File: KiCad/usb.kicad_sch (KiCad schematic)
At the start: 4 parts, among them J16 RJE361882415, J19 USB3_A_Stacked, J20 USB3_IDC, J21 Conn_02x05_Odd_Even

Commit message: Re-annotate components
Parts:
- renumbered J16 to J19, J19 to J22, J20 to J23, J21 to J24
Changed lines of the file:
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@@
 		(dnp no)
 		(fields_autoplaced yes)
-		(property "Reference" "#PWR0219"
+		(property "Reference" "#PWR0273"
 			(at 80.01 59.69 0)
 			(effects
@@
 			(project ""
 				(path "/49abeb3a-c598-45a3-ba6b-595eb04f17a8/aeaf6077-b212-49fa-a33e-8ac7d8738247"
-					(reference "#PWR0219")
+					(reference "#PWR0273")
 					(unit 1)
 				)
@@
 		(on_board yes)
 		(dnp no)
-		(property "Reference" "#PWR0232"
+		(property "Reference" "#PWR0284"
 			(at 248.92 87.63 0)
 			(effects
@@
 			(project "LattePandaMuCluster"
 				(path "/49abeb3a-c598-45a3-ba6b-595eb04f17a8/aeaf6077-b212-49fa-a33e-8ac7d8738247"
-					(reference "#PWR0232")
+					(reference "#PWR0284")
 					(unit 1)
 				)
@@
 		(on_board yes)
 		(dnp no)
-		(property "Reference" "#PWR0228"
+		(property "Reference" "#PWR0276"
 			(at 162.56 78.74 0)
 			(effects
@@
 			(project "LattePandaMuCluster"
 				(path "/49abeb3a-c598-45a3-ba6b-595eb04f17a8/aeaf6077-b212-49fa-a33e-8ac7d8738247"
-					(reference "#PWR0228")
+					(reference "#PWR0276")
 					(unit 1)
 				)
@@
 		(on_board yes)
 		(dnp no)
-		(property "Reference" "#PWR0231"
+		(property "Reference" "#PWR0282"
 			(at 220.98 87.63 0)
 			(effects
@@
 			(project "LattePandaMuCluster"
 				(path "/49abeb3a-c598-45a3-ba6b-595eb04f17a8/aeaf6077-b212-49fa-a33e-8ac7d8738247"
-					(reference "#PWR0231")
+					(reference "#PWR0282")
 					(unit 1)
 				)
@@
 		(dnp no)
 		(fields_autoplaced yes)
-		(property "Reference" "#PWR0221"
+		(property "Reference" "#PWR0275"
 			(at 83.82 163.83 0)
 			(effects
@@
 			(project "LattePandaMuCluster"
 				(path "/49abeb3a-c598-45a3-ba6b-595eb04f17a8/aeaf6077-b212-49fa-a33e-8ac7d8738247"
-					(reference "#PWR0221")
+					(reference "#PWR0275")
 					(unit 1)
 				)
@@
 		(on_board yes)
 		(dnp no)
-		(property "Reference" "#PWR0229"
+		(property "Reference" "#PWR0272"
 			(at 69.85 129.54 0)
 			(effects
@@
 			(project "LattePandaMuCluster"
 				(path "/49abeb3a-c598-45a3-ba6b-595eb04f17a8/aeaf6077-b212-49fa-a33e-8ac7d8738247"
-					(reference "#PWR0229")
+					(reference "#PWR0272")
 					(unit 1)
 				)
@@
 		(dnp no)
 		(fields_autoplaced yes)
-		(property "Reference" "J16"
+		(property "Reference" "J19"
 			(at 189.23 32.3849 0)
 			(effects
@@
 			(project "LattePandaMuCluster"
 				(path "/49abeb3a-c598-45a3-ba6b-595eb04f17a8/aeaf6077-b212-49fa-a33e-8ac7d8738247"
-					(reference "J16")
+					(reference "J19")
 					(unit 3)
 				)
@@
 		(on_board yes)
 		(dnp no)
-		(property "Reference" "#PWR0226"
+		(property "Reference" "#PWR0277"
 			(at 163.83 25.4 0)
 			(effects
@@
 			(project "LattePandaMuCluster"
 				(path "/49abeb3a-c598-45a3-ba6b-595eb04f17a8/aeaf6077-b212-49fa-a33e-8ac7d8738247"
-					(reference "#PWR0226")
+					(reference "#PWR0277")
 					(unit 1)
 				)
@@
 		(on_board yes)
 		(dnp no)
-		(property "Reference" "J19"
+		(property "Reference" "J22"
 			(at 176.53 67.31 0)
 			(effects
@@
 			(project ""
 				(path "/49abeb3a-c598-45a3-ba6b-595eb04f17a8/aeaf6077-b212-49fa-a33e-8ac7d8738247"
-					(reference "J19")
+					(reference "J22")
 					(unit 2)
 				)
@@
 		(on_board yes)
 		(dnp no)
-		(property "Reference" "#PWR0227"
+		(property "Reference" "#PWR0271"
 			(at 69.85 76.2 0)
 			(effects
@@
 			(project "LattePandaMuCluster"
 				(path "/49abeb3a-c598-45a3-ba6b-595eb04f17a8/aeaf6077-b212-49fa-a33e-8ac7d8738247"
-					(reference "#PWR0227")
+					(reference "#PWR0271")
 					(unit 1)
 				)
@@
 		(dnp no)
 		(fields_autoplaced yes)
-		(property "Reference" "J16"
+		(property "Reference" "J19"
 			(at 91.44 32.3849 0)
 			(effects
@@
 			(project "LattePandaMuCluster"
 				(path "/49abeb3a-c598-45a3-ba6b-595eb04f17a8/aeaf6077-b212-49fa-a33e-8ac7d8738247"
-					(reference "J16")
+					(reference "J19")
 					(unit 2)
 				)
@@
 		(dnp no)
 		(fields_autoplaced yes)
-		(property "Reference" "#PWR0222"
+		(property "Reference" "#PWR0281"
 			(at 181.61 163.83 0)
 			(effects
@@
 			(project "LattePandaMuCluster"
 				(path "/49abeb3a-c598-45a3-ba6b-595eb04f17a8/aeaf6077-b212-49fa-a33e-8ac7d8738247"
-					(reference "#PWR0222")
+					(reference "#PWR0281")
 					(unit 1)
 				)
@@
 		(dnp no)
 		(fields_autoplaced yes)
-		(property "Reference" "#PWR0224"
+		(property "Reference" "#PWR0279"
 			(at 176.53 113.03 0)
 			(effects
@@
 			(project "LattePandaMuCluster"
 				(path "/49abeb3a-c598-45a3-ba6b-595eb04f17a8/aeaf6077-b212-49fa-a33e-8ac7d8738247"
-					(reference "#PWR0224")
+					(reference "#PWR0279")
 					(unit 1)
 				)
@@
 		(dnp no)
 		(fields_autoplaced yes)
-		(property "Reference" "#PWR0223"
+		(property "Reference" "#PWR0274"
 			(at 83.82 110.49 0)
 			(effects
@@
 			(project "LattePandaMuCluster"
 				(path "/49abeb3a-c598-45a3-ba6b-595eb04f17a8/aeaf6077-b212-49fa-a33e-8ac7d8738247"
-					(reference "#PWR0223")
+					(reference "#PWR0274")
 					(unit 1)
 				)
@@
 		(dnp no)
 		(fields_autoplaced yes)
-		(property "Reference" "J20"
+		(property "Reference" "J23"
 			(at 95.25 136.5249 0)
 			(effects
@@
 			(project ""
 				(path "/49abeb3a-c598-45a3-ba6b-595eb04f17a8/aeaf6077-b212-49fa-a33e-8ac7d8738247"
-					(reference "J20")
+					(reference "J23")
 					(unit 1)
 				)
@@
 		(dnp no)
 		(fields_autoplaced yes)
-		(property "Reference" "J21"
+		(property "Reference" "J24"
 			(at 234.95 78.74 0)
 			(effects
@@
 			(project ""
 				(path "/49abeb3a-c598-45a3-ba6b-595eb04f17a8/aeaf6077-b212-49fa-a33e-8ac7d8738247"
-					(reference "J21")
+					(reference "J24")
 					(unit 1)
 				)
@@
 		(dnp no)
 		(fields_autoplaced yes)
-		(property "Reference" "#PWR0220"
+		(property "Reference" "#PWR0280"
 			(at 177.8 59.69 0)
 			(effects
@@
 			(project "LattePandaMuCluster"
 				(path "/49abeb3a-c598-45a3-ba6b-595eb04f17a8/aeaf6077-b212-49fa-a33e-8ac7d8738247"
-					(reference "#PWR0220")
+					(reference "#PWR0280")
 					(unit 1)
 				)
@@
 		(dnp no)
 		(fields_autoplaced yes)
-		(property "Reference" "#PWR0233"
+		(property "Reference" "#PWR0283"
 			(at 234.95 106.68 0)
 			(effects
@@
 			(project ""
 				(path "/49abeb3a-c598-45a3-ba6b-595eb04f17a8/aeaf6077-b212-49fa-a33e-8ac7d8738247"
-					(reference "#PWR0233")
+					(reference "#PWR0283")
 					(unit 1)
 				)
@@
 		(dnp no)
 		(fields_autoplaced yes)
-		(property "Reference" "J20"
+		(property "Reference" "J23"
 			(at 193.04 136.5249 0)
 			(effects
@@
 			(project ""
 				(path "/49abeb3a-c598-45a3-ba6b-595eb04f17a8/aeaf6077-b212-49fa-a33e-8ac7d8738247"
-					(reference "J20")
+					(reference "J23")
 					(unit 2)
 				)
@@
 		(on_board yes)
 		(dnp no)
-		(property "Reference" "#PWR0230"
+		(property "Reference" "#PWR0278"
 			(at 167.64 129.54 0)
 			(effects
@@
 			(project "LattePandaMuCluster"
 				(path "/49abeb3a-c598-45a3-ba6b-595eb04f17a8/aeaf6077-b212-49fa-a33e-8ac7d8738247"
-					(reference "#PWR0230")
+					(reference "#PWR0278")
 					(unit 1)
 				)
@@
 		(on_board yes)
 		(dnp no)
-		(property "Reference" "J19"
+		(property "Reference" "J22"
 			(at 83.82 64.77 0)
 			(effects
@@
 			(project ""
 				(path "/49abeb3a-c598-45a3-ba6b-595eb04f17a8/aeaf6077-b212-49fa-a33e-8ac7d8738247"
-					(reference "J19")
+					(reference "J22")
 					(unit 1)
 				)
@@
 		(on_board yes)
 		(dnp no)
-		(property "Reference" "#PWR0225"
+		(property "Reference" "#PWR0270"
 			(at 66.04 25.4 0)
 			(effects
@@
 			(project ""
 				(path "/49abeb3a-c598-45a3-ba6b-595eb04f17a8/aeaf6077-b212-49fa-a33e-8ac7d8738247"
-					(reference "#PWR0225")
-					(unit 1)
-				)
+					(reference "#PWR0270")
+					(unit 1)
+				)

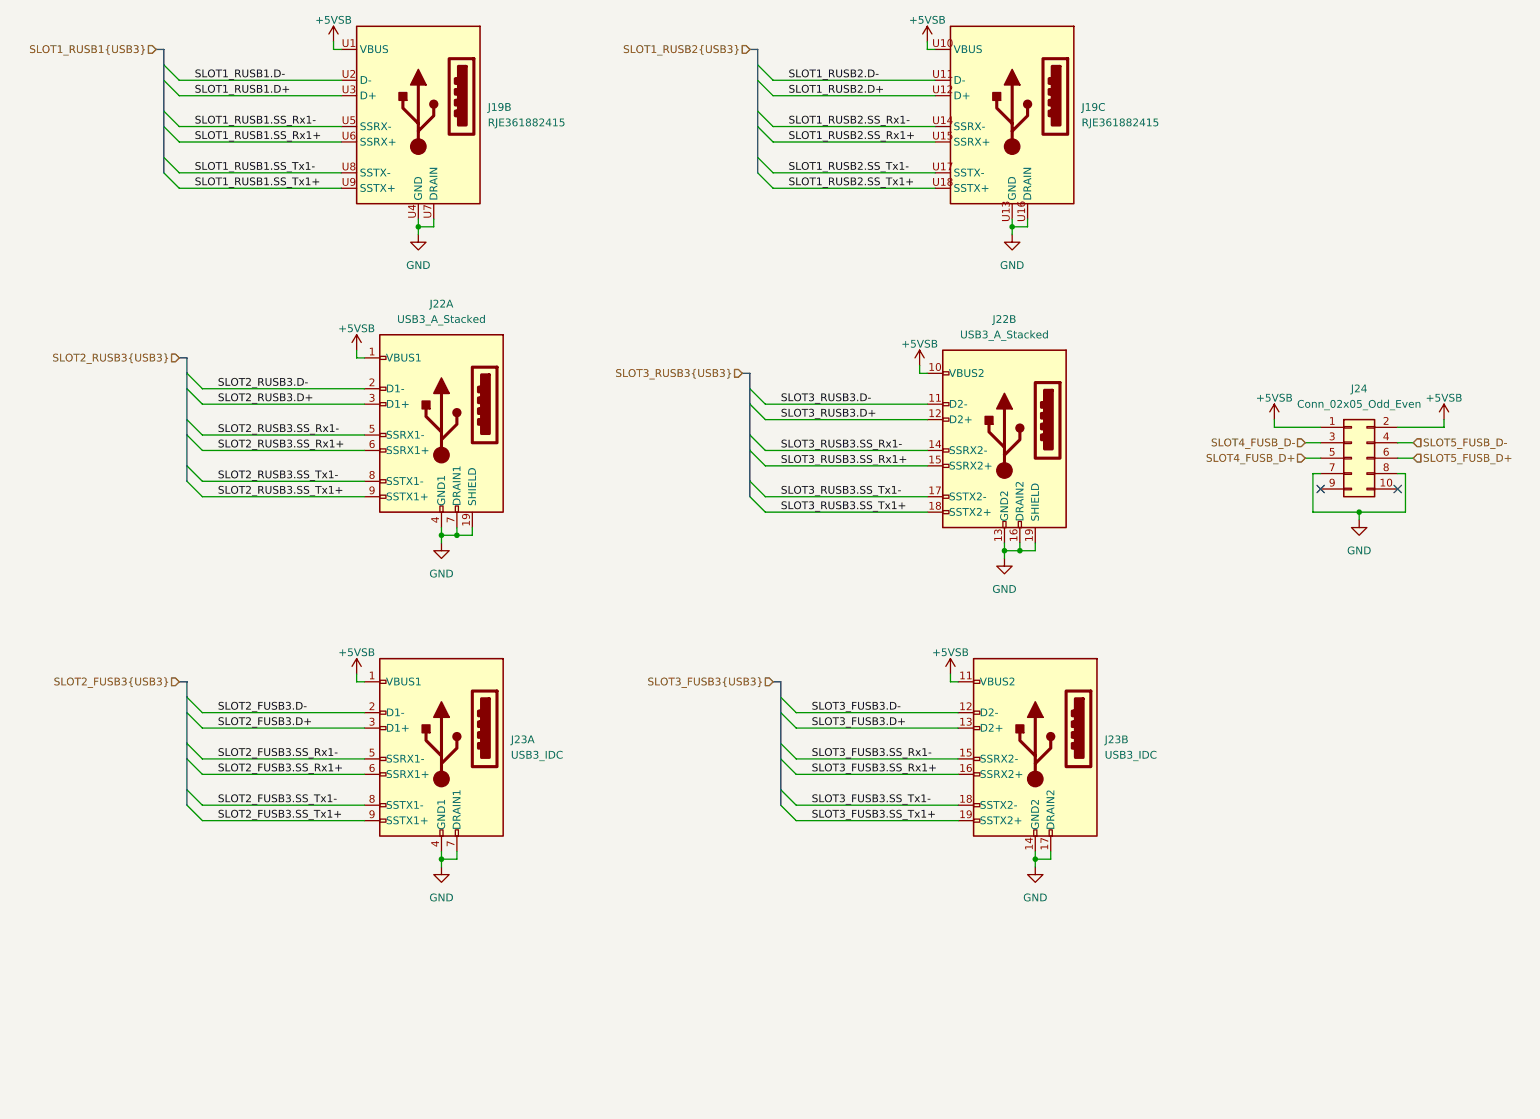
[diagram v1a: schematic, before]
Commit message: Add TVS diodes for ESD protection
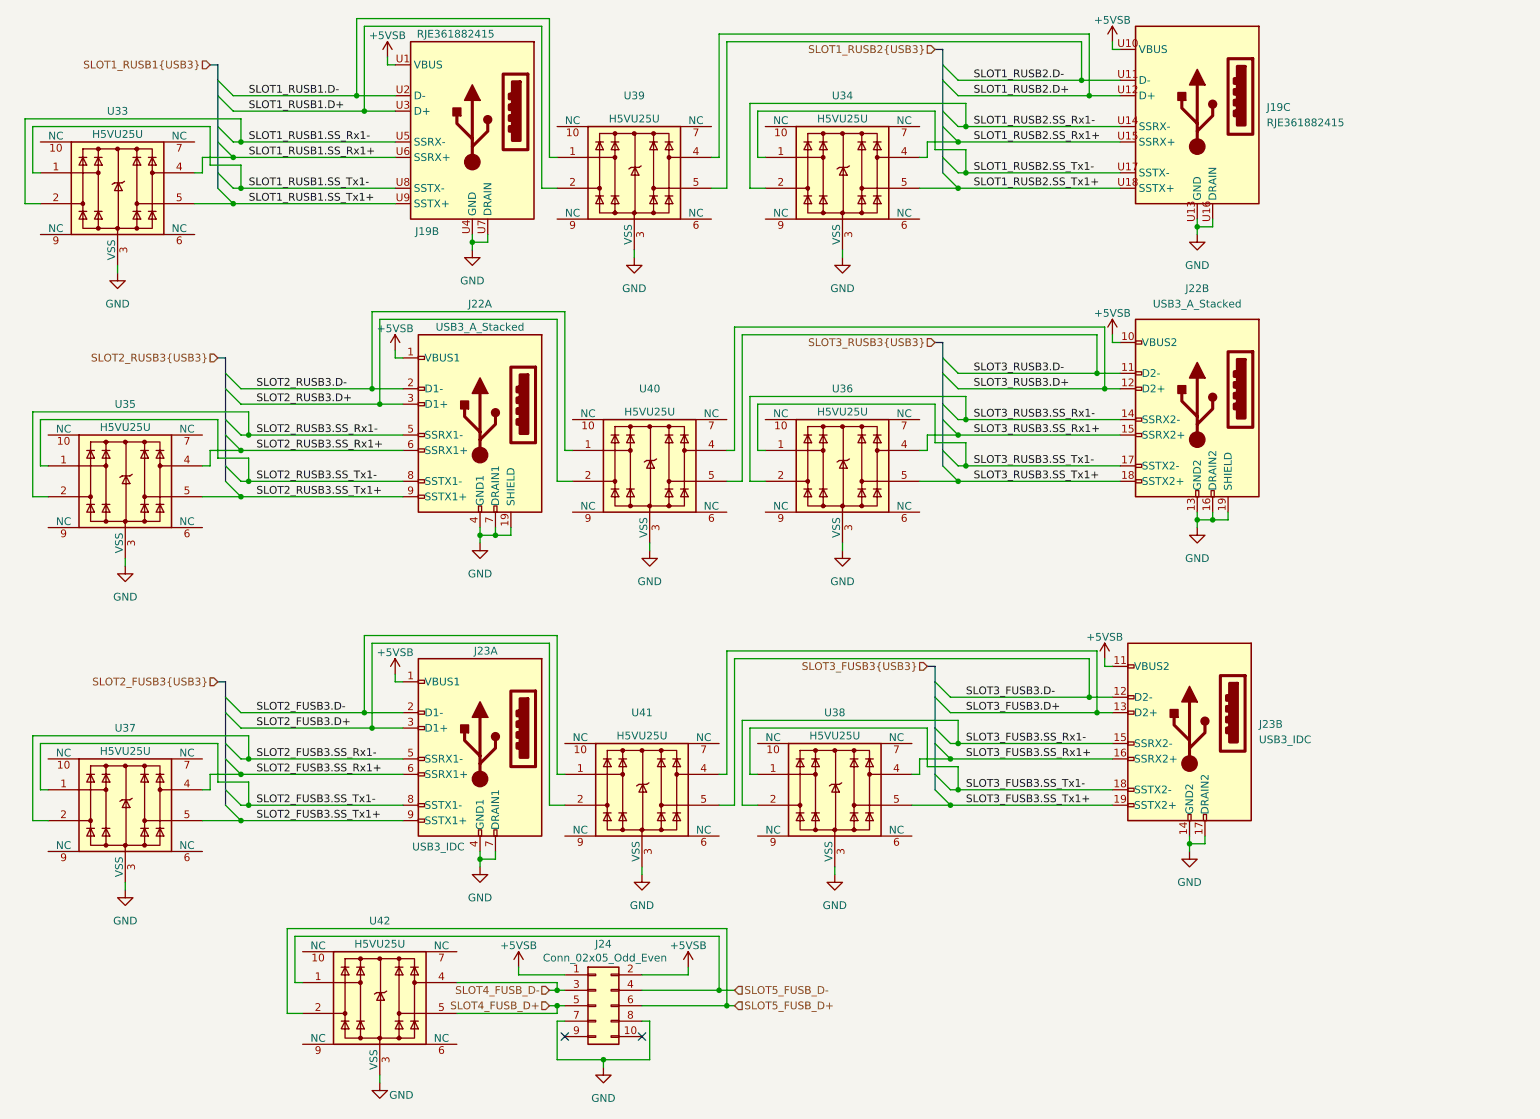
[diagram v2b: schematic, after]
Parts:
- added U33, U34, U35, U36, U37, U38, U39, U40, U41, U42: H5VU25U, Package_DFN_QFN:Diodes_UDFN-10_1.0x2.5mm_P0.5mm, symbol Power_Protection:D3V3XA4B10LP
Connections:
- net GND: now also U33.3 (VSS), U33.8 (VSS), U34.3 (VSS), U34.8 (VSS), U35.3 (VSS), U35.8 (VSS), U36.3 (VSS), U36.8 (VSS), U37.3 (VSS), U37.8 (VSS), U38.3 (VSS), U38.8 (VSS), U39.3 (VSS), U39.8 (VSS), U40.3 (VSS), U40.8 (VSS), U41.3 (VSS), U41.8 (VSS), U42.3 (VSS), U42.8 (VSS)
- net SLOT1_RUSB1.D+: now also U39.2
- net SLOT1_RUSB1.D-: now also U39.1
- net SLOT1_RUSB1.SS_Rx1+: now also U33.4
- net SLOT1_RUSB1.SS_Rx1-: now also U33.2
- net SLOT1_RUSB1.SS_Tx1+: now also U33.5
- net SLOT1_RUSB1.SS_Tx1-: now also U33.1
- net SLOT1_RUSB2.D+: now also U39.4
- net SLOT1_RUSB2.D-: now also U39.5
- net SLOT1_RUSB2.SS_Rx1+: now also U34.4
- net SLOT1_RUSB2.SS_Rx1-: now also U34.2
- net SLOT1_RUSB2.SS_Tx1+: now also U34.5
- net SLOT1_RUSB2.SS_Tx1-: now also U34.1
- net SLOT2_FUSB3.D+: now also U41.2
- net SLOT2_FUSB3.D-: now also U41.1
- net SLOT2_FUSB3.SS_Rx1+: now also U37.4
- net SLOT2_FUSB3.SS_Rx1-: now also U37.2
- net SLOT2_FUSB3.SS_Tx1+: now also U37.5
- net SLOT2_FUSB3.SS_Tx1-: now also U37.1
- net SLOT2_RUSB3.D+: now also U40.2
- net SLOT2_RUSB3.D-: now also U40.1
- net SLOT2_RUSB3.SS_Rx1+: now also U35.4
- net SLOT2_RUSB3.SS_Rx1-: now also U35.2
- net SLOT2_RUSB3.SS_Tx1+: now also U35.5
- net SLOT2_RUSB3.SS_Tx1-: now also U35.1
- net SLOT3_FUSB3.D+: now also U41.4
- net SLOT3_FUSB3.D-: now also U41.5
- net SLOT3_FUSB3.SS_Rx1+: now also U38.4
- net SLOT3_FUSB3.SS_Rx1-: now also U38.2
- net SLOT3_FUSB3.SS_Tx1+: now also U38.5
- net SLOT3_FUSB3.SS_Tx1-: now also U38.1
- net SLOT3_RUSB3.D+: now also U40.4
- net SLOT3_RUSB3.D-: now also U40.5
- net SLOT3_RUSB3.SS_Rx1+: now also U36.4
- net SLOT3_RUSB3.SS_Rx1-: now also U36.2
- net SLOT3_RUSB3.SS_Tx1+: now also U36.5
- net SLOT3_RUSB3.SS_Tx1-: now also U36.1
- net SLOT4_FUSB_D+: now also U42.5
- net SLOT4_FUSB_D-: now also U42.4
- net SLOT5_FUSB_D+: now also U42.2
- net SLOT5_FUSB_D-: now also U42.1
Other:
- moved on the sheet: J19B, J19C, J22A, J22B, J23A, J23B, J24

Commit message: Fix esd diodes, add some footprints.
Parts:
- J19: footprint (none) -> RJE361882145:AMPHENOL_RJE361882415
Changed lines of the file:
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@@
 			)
 		)
-		(property "Footprint" ""
+		(property "Footprint" "RJE361882145:AMPHENOL_RJE361882415"
 			(at 208.28 17.78 0)
 			(effects
@@
 			)
 		)
-		(property "Footprint" ""
+		(property "Footprint" "RJE361882145:AMPHENOL_RJE361882415"
 			(at 88.9 20.32 0)
 			(effects

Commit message: Add more footprints
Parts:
- removed J24: Conn_02x05_Odd_Even, symbol Connector_Generic:Conn_02x05_Odd_Even
- added J24: Conn_01x05, Connector_PinHeader_2.54mm:PinHeader_1x05_P2.54mm_Vertical, symbol Connector_Generic:Conn_01x05
- added J27: Conn_01x04, Connector_PinHeader_2.54mm:PinHeader_1x04_P2.54mm_Vertical, symbol Connector_Generic:Conn_01x04
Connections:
- net +5VSB: now also J24.1 (Pin_1), J27.1 (Pin_1)
- net GND: now also J24.4 (Pin_4), J27.4 (Pin_4)
- net SLOT4_FUSB_D+: now also J24.3 (Pin_3)
- net SLOT4_FUSB_D-: now also J24.2 (Pin_2)
- net SLOT5_FUSB_D+: now also J27.3 (Pin_3)
- net SLOT5_FUSB_D-: now also J27.2 (Pin_2)
- no-connect marks 2 -> 1
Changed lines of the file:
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@@
 	)
 	(no_connect
-		(at 116.84 185.42)
-	)
-	(no_connect
 		(at 104.14 185.42)
 	)
@@
 	)
 	(symbol
+		(lib_id "Connector_Generic:Conn_01x05")
+		(at 109.22 180.34 0)
+		(unit 1)
+		(exclude_from_sim no)
+		(in_bom yes)
+		(on_board yes)
+		(dnp no)
+		(property "Reference" "J24"
+			(at 110.49 185.928 0)
+			(effects
+				(font
+					(size 1.27 1.27)
+				)
+				(justify left)
+			)
+		)
+		(property "Value" "Conn_01x05"
+			(at 103.378 187.96 0)
+			(effects
+				(font
+					(size 1.27 1.27)
+				)
+				(justify left)
+			)
+		)
+		(property "Footprint" "Connector_PinHeader_2.54mm:PinHeader_1x05_P2.54mm_Vertical"
+			(at 109.22 180.34 0)
+			(effects
+				(font
+					(size 1.27 1.27)
+				)
+				(hide yes)
+			)
+		)
+		(property "Datasheet" "~"
+			(at 109.22 180.34 0)
+			(effects
+				(font
+					(size 1.27 1.27)
+				)
+				(hide yes)
+			)
+		)
+		(property "Description" "Generic connector, single row, 01x05, script generated (kicad-library-utils/schlib/autogen/connector/)"
+			(at 109.22 180.34 0)
+			(effects
+				(font
+					(size 1.27 1.27)
+				)
+				(hide yes)
+			)
+		)
+		(pin "3"
+		)
+		(pin "4"
+		)
+		(pin "2"
+		)
+		(pin "1"
+		)
+		(pin "5"
+		)
+		(instances
+			(project ""
+				(path "/49abeb3a-c598-45a3-ba6b-595eb04f17a8/aeaf6077-b212-49fa-a33e-8ac7d8738247"
+					(reference "J24")
+					(unit 1)
+				)
+			)
+		)
+	)
+	(symbol
 		(lib_id "power:+5V")
 		(at 124.46 173.99 0)
@@
 	)
 	(symbol
-		(lib_id "Connector_Generic:Conn_02x05_Odd_Even")
-		(at 109.22 180.34 0)
+		(lib_id "Connector_Generic:Conn_01x04")
+		(at 111.76 177.8 0)
+		(mirror y)
 		(unit 1)
 		(exclude_from_sim no)
@@
 		(on_board yes)
 		(dnp no)
-		(property "Reference" "J24"
-			(at 110.49 170.18 0)
+		(property "Reference" "J27"
+			(at 110.744 170.942 0)
 			(effects
 				(font
@@
 			)
 		)
-		(property "Value" "Conn_02x05_Odd_Even"
-			(at 110.744 172.466 0)
+		(property "Value" "Conn_01x04"
+			(at 111.76 172.72 0)
 			(effects
 				(font
@@
 			)
 		)
-		(property "Footprint" ""
-			(at 109.22 180.34 0)
+		(property "Footprint" "Connector_PinHeader_2.54mm:PinHeader_1x04_P2.54mm_Vertical"
+			(at 111.76 177.8 0)
 			(effects
 				(font
@@
 		)
 		(property "Datasheet" "~"
-			(at 109.22 180.34 0)
+			(at 111.76 177.8 0)
 			(effects
 				(font
@@
 			)
 		)
-		(property "Description" "Generic connector, double row, 02x05, odd/even pin numbering scheme (row 1 odd numbers, row 2 even numbers), script generated (kicad-library-utils/schlib/autogen/connector/)"
-			(at 109.22 180.34 0)
+		(property "Description" "Generic connector, single row, 01x04, script generated (kicad-library-utils/schlib/autogen/connector/)"
+			(at 111.76 177.8 0)
 			(effects
 				(font
@@
 		(pin "1"
 		)
-		(pin "10"
-		)
-		(pin "8"
-		)
-		(pin "7"
-		)
-		(pin "5"
-		)
-		(pin "6"
-		)
-		(pin "3"
-		)
 		(pin "2"
 		)
-		(pin "9"
-		)
 		(pin "4"
 		)
+		(pin "3"
+		)
 		(instances
 			(project ""
 				(path "/49abeb3a-c598-45a3-ba6b-595eb04f17a8/aeaf6077-b212-49fa-a33e-8ac7d8738247"
-					(reference "J24")
+					(reference "J27")
 					(unit 1)
 				)

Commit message: Add USB Type E Header Footprint
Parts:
- J19: symbol custom:1xRJ45+2xUSB3 -> Custom:1xRJ45+2xUSB3
- J23: symbol custom:USB3_IDC -> Custom:USB3_IDC
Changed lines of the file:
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@@
 	)
 	(symbol
-		(lib_id "custom:1xRJ45+2xUSB3")
+		(lib_id "Custom:1xRJ45+2xUSB3")
 		(at 208.28 17.78 0)
 		(mirror y)
@@
 	)
 	(symbol
-		(lib_id "custom:1xRJ45+2xUSB3")
+		(lib_id "Custom:1xRJ45+2xUSB3")
 		(at 88.9 20.32 0)
 		(mirror y)
@@
 	)
 	(symbol
-		(lib_id "custom:USB3_IDC")
+		(lib_id "Custom:USB3_IDC")
 		(at 90.17 137.16 0)
 		(mirror y)
@@
 	)
 	(symbol
-		(lib_id "custom:USB3_IDC")
+		(lib_id "Custom:USB3_IDC")
 		(at 207.01 134.62 0)
 		(mirror y)

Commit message: Add footprintss from LCSC
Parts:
- J22: footprint (none) -> EasyEDA2KiCAD:USB-A-TH_HC-USB3.0-L175-2X1-J
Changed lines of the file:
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@@
 			)
 		)
-		(property "Footprint" ""
+		(property "Footprint" "EasyEDA2KiCAD:USB-A-TH_HC-USB3.0-L175-2X1-J"
 			(at 204.47 78.74 0)
 			(effects
@@
 			)
 		)
-		(property "Footprint" ""
+		(property "Footprint" "EasyEDA2KiCAD:USB-A-TH_HC-USB3.0-L175-2X1-J"
 			(at 86.36 81.28 0)
 			(effects

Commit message: Finish fixing footprints
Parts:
- renumbered J19 to J20, J27 to J24, J24 to J25, U39 to U28, U34 to U29, U33 to U30, U40 to U31, U36 to U32, U35 to U33, U41 to U34, U38 to U35, U37 to U36, U42 to U37
